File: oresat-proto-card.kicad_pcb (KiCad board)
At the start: 4 copper layers, 99.8 x 97.2 mm, 125 parts, among them J1 TFM-110-01-L-D-RA, J2 1909763-1, J3 1909763-1, J4 1909763-1, J6 TFM-120-01-L-D-RA, J7 ORESAT-DEBUG-CONNECTOR-ALL, Q1 DMP2240UDM, Q2 DMP3050LVT-7, Q7 DMP3050LVT-7, Q8 PMV45EN2R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

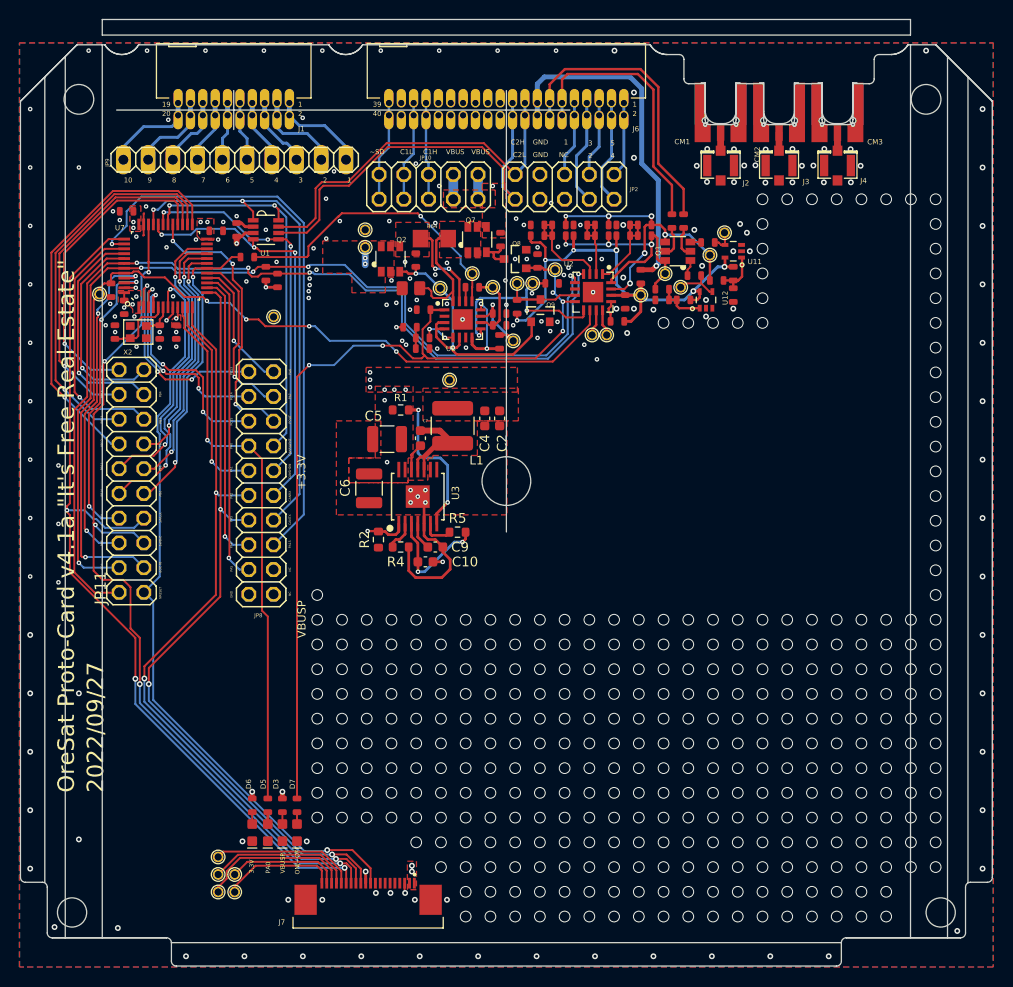
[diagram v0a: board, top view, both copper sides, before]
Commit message: Reverted All Changes to V0.3
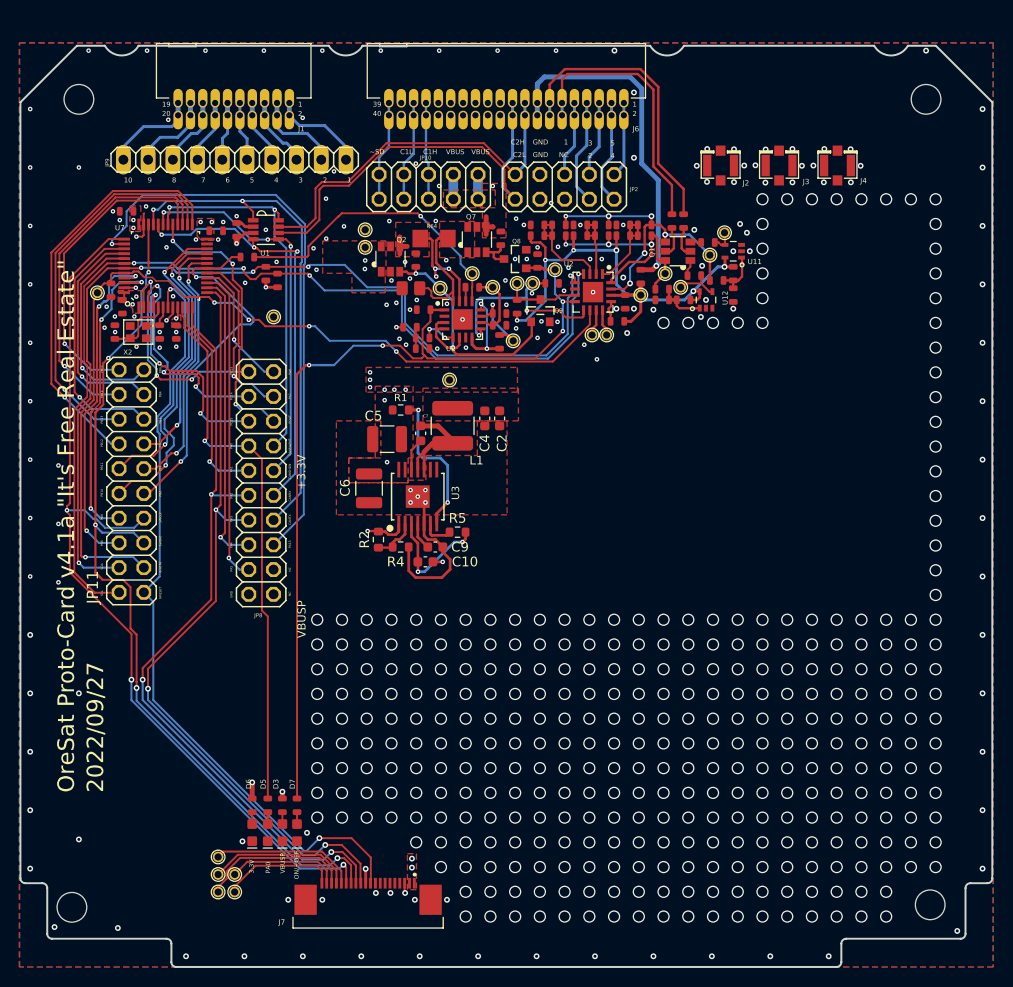
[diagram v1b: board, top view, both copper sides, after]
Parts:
- removed CM1, CM2, CM3: 73300-0020, oresat-proto-card:J-MOLEX-SMPM-073300-003X
- removed U$1: , oresat-proto-card:ORESAT-CARD-V1.3-GENERIC-3RF
- added ?: , , F.Cu at (103.9, 147.6)
- added ?: , , F.Cu at (192.0, 147.3)
- moved C7 0.50 mm to (139.7, 98.9)
- moved TP25 0.26 mm to (106.5, 84.5)
- moved C13 0.19 mm to (109.1, 85.9)
- moved R62 0.13 mm to (147.9, 78.9)
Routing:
- net VBUSP: track 35.9 -> 29.2 mm, vias 15 -> 14
- net /Microcontroller/PB0/POUTPROT: track 31.5 -> 37.5 mm
- net (no net): track 0.00 -> 5.02 mm
- net Net-(CM3-PadRF): track 1.90 -> 0.00 mm
- net Net-(CM2-PadRF): track 1.90 -> 0.00 mm
- net Net-(CM1-PadRF): track 1.90 -> 0.00 mm
- net /Microcontroller/PA3/USART2_RX: track 79.8 -> 81.5 mm
- net /Microcontroller/NRESET: track 78.5 -> 80.1 mm
- net Net-(R2-Pad1): track 3.17 -> 4.66 mm
- net /Microcontroller/PC14: track 22.0 -> 23.4 mm
- net /Microcontroller/PA2/USART2_TX: track 78.4 -> 79.8 mm
- net /Microcontroller/PC13: track 21.9 -> 23.0 mm
- net /Microcontroller/PB9: track 30.9 -> 31.9 mm
- net /Microcontroller/PA9/CAN_SILENT: track 40.2 -> 39.3 mm
- net /Microcontroller/PB10: track 32.2 -> 33.1 mm
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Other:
- board size 99.8 x 97.2 mm -> 99.8 x 94.6 mm

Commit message: Return of the Holes
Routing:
- net (no net): vias 268 -> 380

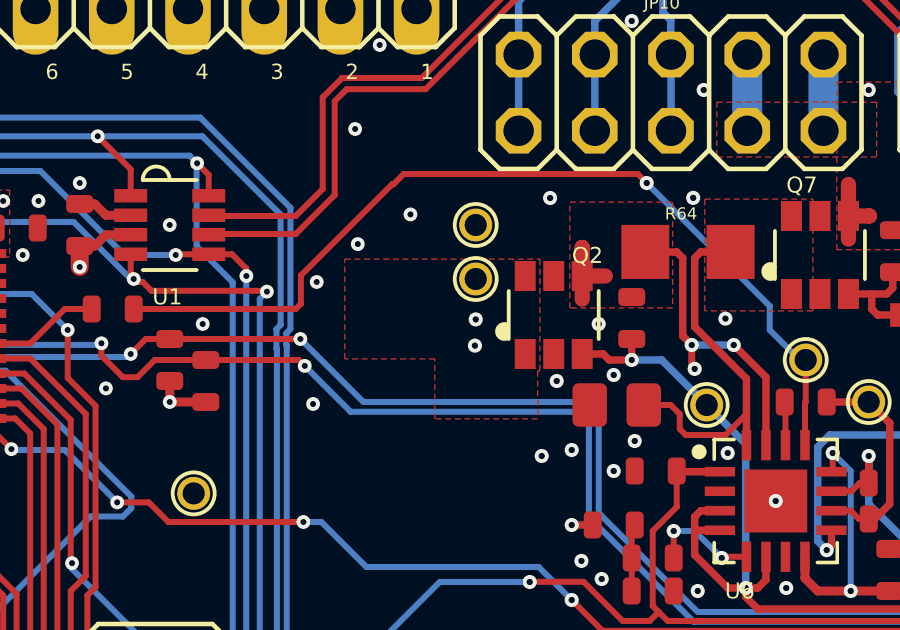
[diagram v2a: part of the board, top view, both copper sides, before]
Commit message: V0.4 BOM Updates and Footprint Fixes
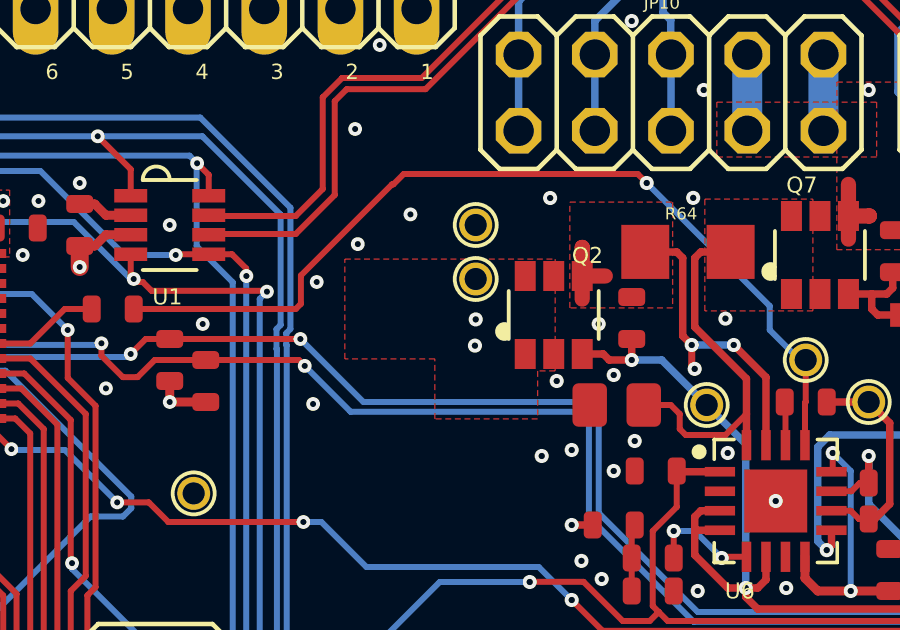
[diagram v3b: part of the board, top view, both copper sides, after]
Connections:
- Q2 pad 1: /Power/CB_CTRL -> VBUSP
- Q2 pad 2: (no net) -> VBUSP
- Q2 pad 3: (no net) -> /Power/CB_CTRL
- Q2 pad 4: (no net) -> Net-(Q2-Pad5)
- Q2 pad 5: Net-(Q2-Pad5) -> VBUSP
- Q7 pad 1: Net-(Q7-Pad1) -> Net-(C1-Pad1)
- Q7 pad 2: (no net) -> Net-(C1-Pad1)
- Q7 pad 3: (no net) -> Net-(Q7-Pad1)
- Q7 pad 4: (no net) -> VBUS
- Q7 pad 5: VBUS -> Net-(C1-Pad1)
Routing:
- net (no net): track 5.02 -> 0.00 mm
- net VBUS: track 5.08 -> 7.61 mm
- net Net-(Q2-Pad5): track 10.4 -> 12.8 mm
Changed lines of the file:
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@@
       ) (layer "F.Fab") (width 0) (fill solid))
     (pad "1" smd rect (at -0.95 1.3) (size 0.7 1) (layers "F.Cu" "F.Paste")
-      (net 99 "Net-(Q7-Pad1)") (pinfunction "G") (pintype "passive") (solder_mask_margin 0.0635))
+      (net 2 "Net-(C1-Pad1)") (pinfunction "G") (pintype "passive") (solder_mask_margin 0.0635))
     (pad "2" smd rect (at 0 1.3) (size 0.7 1) (layers "F.Cu" "F.Paste")
-      (solder_mask_margin 0.0635))
+      (net 2 "Net-(C1-Pad1)") (solder_mask_margin 0.0635))
     (pad "3" smd rect (at 0.95 1.3) (size 0.7 1) (layers "F.Cu" "F.Paste")
-      (solder_mask_margin 0.0635))
+      (net 99 "Net-(Q7-Pad1)") (solder_mask_margin 0.0635))
     (pad "4" smd rect (at 0.95 -1.3) (size 0.7 1) (layers "F.Cu" "F.Paste")
-      (solder_mask_margin 0.0635))
+      (net 120 "VBUS") (solder_mask_margin 0.0635))
     (pad "5" smd rect (at 0 -1.3) (size 0.7 1) (layers "F.Cu" "F.Paste")
-      (net 120 "VBUS") (pinfunction "S") (pintype "passive") (solder_mask_margin 0.0635))
+      (net 2 "Net-(C1-Pad1)") (pinfunction "S") (pintype "passive") (solder_mask_margin 0.0635))
     (pad "6" smd rect (at -0.95 -1.3) (size 0.7 1) (layers "F.Cu" "F.Paste")
       (net 2 "Net-(C1-Pad1)") (pinfunction "D") (pintype "passive") (solder_mask_margin 0.0635))
@@
       ) (layer "F.Fab") (width 0) (fill solid))
     (pad "1" smd rect (at -0.95 1.3) (size 0.7 1) (layers "F.Cu" "F.Paste")
-      (net 98 "/Power/CB_CTRL") (pinfunction "G") (pintype "passive") (solder_mask_margin 0.0635))
+      (net 127 "VBUSP") (pinfunction "G") (pintype "passive") (solder_mask_margin 0.0635))
     (pad "2" smd rect (at 0 1.3) (size 0.7 1) (layers "F.Cu" "F.Paste")
-      (solder_mask_margin 0.0635))
+      (net 127 "VBUSP") (solder_mask_margin 0.0635))
     (pad "3" smd rect (at 0.95 1.3) (size 0.7 1) (layers "F.Cu" "F.Paste")
-      (solder_mask_margin 0.0635))
+      (net 98 "/Power/CB_CTRL") (solder_mask_margin 0.0635))
     (pad "4" smd rect (at 0.95 -1.3) (size 0.7 1) (layers "F.Cu" "F.Paste")
-      (solder_mask_margin 0.0635))
+      (net 97 "Net-(Q2-Pad5)") (solder_mask_margin 0.0635))
     (pad "5" smd rect (at 0 -1.3) (size 0.7 1) (layers "F.Cu" "F.Paste")
-      (net 97 "Net-(Q2-Pad5)") (pinfunction "S") (pintype "passive") (solder_mask_margin 0.0635))
+      (net 127 "VBUSP") (pinfunction "S") (pintype "passive") (solder_mask_margin 0.0635))
     (pad "6" smd rect (at -0.95 -1.3) (size 0.7 1) (layers "F.Cu" "F.Paste")
       (net 127 "VBUSP") (pinfunction "D") (pintype "passive") (solder_mask_margin 0.0635))
@@
     (effects (font (size 0.46 0.46) (thickness 0.04)) (justify left bottom))
   )
-  (segment (start 137.55 80.475) (end 137.55 79.7047) (width 0.508) (layer "F.Cu") (net 0))
-  (segment (start 146.425 77.7036) (end 146.425 76.65) (width 0.508) (layer "F.Cu") (net 0))
-  (segment (start 137.55 79.7047) (end 137.5511 79.7036) (width 0.508) (layer "F.Cu") (net 0))
-  (segment (start 137.5511 79.7036) (end 138.3214 79.7036) (width 0.508) (layer "F.Cu") (net 0))
-  (segment (start 147.1214 77.7036) (end 147.125 77.7) (width 0.508) (layer "F.Cu") (net 0))
-  (segment (start 146.425 77.7036) (end 147.1214 77.7036) (width 0.508) (layer "F.Cu") (net 0))
-  (segment (start 146.425 77.7036) (end 146.425 78.475) (width 0.508) (layer "F.Cu") (net 0))
-  (segment (start 137.5511 79.7036) (end 137.5511 78.7511) (width 0.508) (layer "F.Cu") (net 0))
-  (segment (start 137.5511 78.7511) (end 137.55 78.75) (width 0.508) (layer "F.Cu") (net 0))
   (via (at 187.4 100.25) (size 1.26) (drill 1) (layers "F.Cu" "B.Cu") (net 0))
   (via (at 184.86 115.49) (size 1.26) (drill 1) (layers "F.Cu" "B.Cu") (net 0))
@@
   (segment (start 163.4011 76.6036) (end 159.0011 76.6036) (width 0.2) (layer "B.Cu") (net 96))
   (segment (start 167.3011 78.5036) (end 169.4011 80.6036) (width 0.25) (layer "B.Cu") (net 96))
+  (segment (start 137.55 80.475) (end 137.55 79.7047) (width 0.508) (layer "F.Cu") (net 97))
   (segment (start 142.6011 82.0036) (end 143.6761 83.0786) (width 0.25) (layer "F.Cu") (net 97))
   (segment (start 140.9011 79.1036) (end 140.9011 81.7036) (width 0.25) (layer "F.Cu") (net 97))
   (segment (start 139.6791 78.9036) (end 140.7011 78.9036) (width 0.25) (layer "F.Cu") (net 97))
+  (segment (start 137.55 79.7047) (end 137.5511 79.7036) (width 0.508) (layer "F.Cu") (net 97))
   (segment (start 143.6761 83.0786) (end 143.6761 85.344) (width 0.25) (layer "F.Cu") (net 97))
   (segment (start 141.2011 82.7011) (end 141.3 82.8) (width 0.23495) (layer "F.Cu") (net 97))
+  (segment (start 137.5511 79.7036) (end 138.3214 79.7036) (width 0.508) (layer "F.Cu") (net 97))
   (segment (start 140.9011 81.7036) (end 141.2011 82.0036) (width 0.25) (layer "F.Cu") (net 97))
   (segment (start 141.2011 82.0036) (end 141.2011 82.7011) (width 0.23495) (layer "F.Cu") (net 97))
+  (segment (start 137.5511 79.7036) (end 137.5511 78.7511) (width 0.508) (layer "F.Cu") (net 97))
   (segment (start 140.7011 78.9036) (end 140.9011 79.1036) (width 0.25) (layer "F.Cu") (net 97))
+  (segment (start 137.5511 78.7511) (end 137.55 78.75) (width 0.508) (layer "F.Cu") (net 97))
   (via (at 142.6011 82.0036) (size 0.47) (drill 0.21) (layers "F.Cu" "B.Cu") (net 97))
   (via (at 141.3 82.8) (size 0.47) (drill 0.21) (layers "F.Cu" "B.Cu") (net 97))
@@
   (segment (start 157.7261 86.2632) (end 157.7261 87.7786) (width 0.25) (layer "F.Cu") (net 119))
   (segment (start 157.7261 87.7786) (end 157.3011 88.2036) (width 0.25) (layer "F.Cu") (net 119))
+  (segment (start 146.425 77.7036) (end 146.425 76.65) (width 0.508) (layer "F.Cu") (net 120))
+  (segment (start 147.1214 77.7036) (end 147.125 77.7) (width 0.508) (layer "F.Cu") (net 120))
+  (segment (start 146.425 77.7036) (end 147.1214 77.7036) (width 0.508) (layer "F.Cu") (net 120))
+  (segment (start 146.425 77.7036) (end 146.425 78.475) (width 0.508) (layer "F.Cu") (net 120))
   (segment (start 145.5911 72.3236) (end 145.5911 74.8636) (width 1) (layer "B.Cu") (net 120))
   (segment (start 143.0511 72.3236) (end 143.0511 74.8636) (width 1) (layer "B.Cu") (net 120))
@@
     (polygon
       (pts
-        (xy 136.1396 82.8671)
+        (xy 136.6496 82.8671)
         (xy 136.0646 82.8671)
         (xy 136.0646 84.4671)
@@
         (xy 129.6376 82.4671)
         (xy 129.6376 79.1401)
-        (xy 136.1396 79.1401)
+        (xy 136.6496 79.1401)
       )
     )

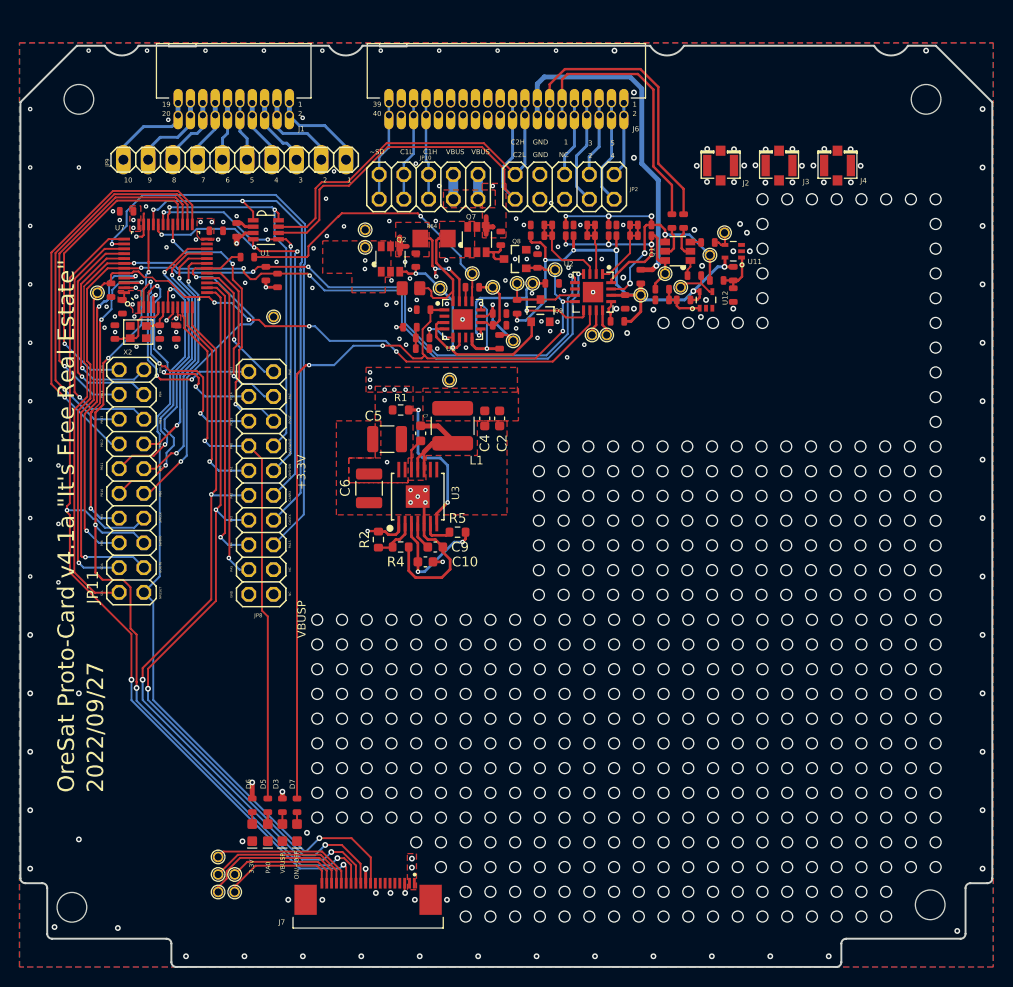
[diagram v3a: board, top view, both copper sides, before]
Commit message: Moved Some Holes
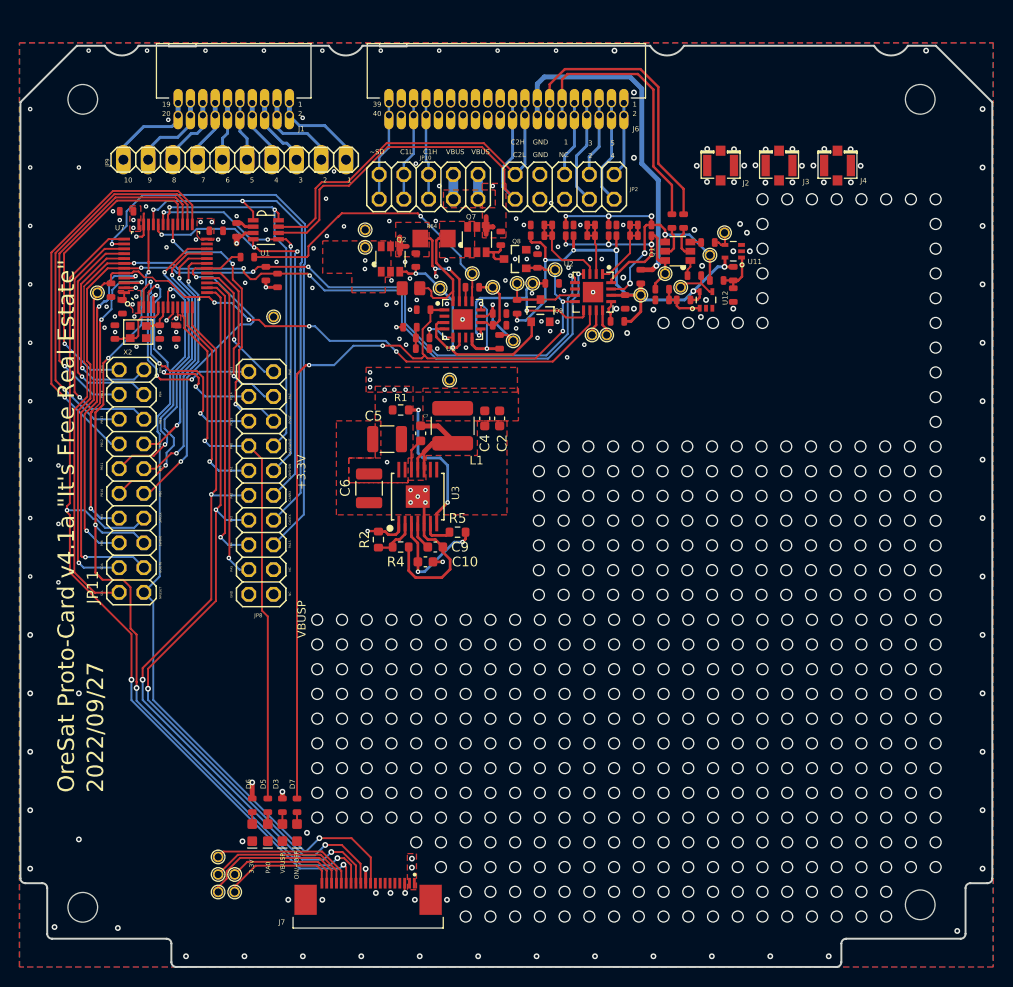
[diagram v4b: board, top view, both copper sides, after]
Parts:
- moved ? 1.11 mm to (105.0, 147.6)
- moved ? 1.02 mm to (191.0, 147.3)
- moved H2 0.60 mm to (191.0, 64.6)
- moved H3 0.40 mm to (105.0, 64.6)
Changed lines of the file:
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@@
   )
   (footprint "oresat-proto-card:STAND-OFF-TIGHT" (layer "F.Cu")
-    (at 191.6011 64.6036)
+    (at 191 64.6036)
     (descr "<h3>Standoff (#4 Screw) - Tight fit around screw body</h3>\n<p>This is the mechanical footprint for a #4 phillips button head screw. Use the keepout ring to avoid running the screw head into surrounding components.</p>\n<h4>Devices Using</h4>\n<ul><li>STAND-OFF</li></ul>")
     (property "Sheetfile" "Connectors.kicad_sch")
@@
   )
   (footprint "oresat-proto-card:STAND-OFF-TIGHT" (layer "F.Cu")
-    (at 104.6011 64.6036)
+    (at 105 64.6036)
     (descr "<h3>Standoff (#4 Screw) - Tight fit around screw body</h3>\n<p>This is the mechanical footprint for a #4 phillips button head screw. Use the keepout ring to avoid running the screw head into surrounding components.</p>\n<h4>Devices Using</h4>\n<ul><li>STAND-OFF</li></ul>")
     (property "Sheetfile" "Connectors.kicad_sch")
@@
   )
   (footprint "" (layer "F.Cu")
-    (at 103.886 147.574)
+    (at 105 147.574)
     (fp_text reference "" (at 0 0) (layer "F.SilkS")
       (effects (font (size 1.27 1.27) (thickness 0.15)))
@@
   )
   (footprint "" (layer "F.Cu")
-    (at 192.024 147.32)
+    (at 191 147.32)
     (fp_text reference "" (at 0 0) (layer "F.SilkS")
       (effects (font (size 1.27 1.27) (thickness 0.15)))
